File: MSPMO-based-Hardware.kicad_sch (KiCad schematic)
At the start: 0 parts

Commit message: created MSPMOG3507SPTR symbol
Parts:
- added U1: ~, Package_QFP:LQFP-48-1EP_7x7mm_P0.5mm_EP3.6x3.6mm_ThermalVias, symbol MSPMOG3507SPTR:MSPMOG3507SPTR
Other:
- title: Schematic-1 -> MSPMO-Hardware
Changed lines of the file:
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@@
 	(paper "A4")
 	(title_block
-		(title "Schematic-1")
-		(date "2026-02-09")
+		(title "MSPMO-Hardware")
+		(date "2026-02-16")
 		(company "Odari-Designs")
 	)
+	(symbol
+		(lib_id "MSPMOG3507SPTR:MSPMOG3507SPTR")
+		(at 133.35 50.8 0)
+		(unit 1)
+		(exclude_from_sim no)
+		(in_bom yes)
+		(on_board yes)
+		(dnp no)
+		(property "Reference" "U1"
+			(at 175.514 102.616 0)
+			(effects
+				(font
+					(size 1.27 1.27)
+				)
+				(justify left)
+			)
+		)
+		(property "Value" "~"
+			(at 150.7333 139.7 0)
+			(effects
+				(font
+					(size 1.27 1.27)
+				)
+				(justify left)
+			)
+		)
+		(property "Footprint" "Package_QFP:LQFP-48-1EP_7x7mm_P0.5mm_EP3.6x3.6mm_ThermalVias"
+			(at 133.35 50.8 0)
+			(effects
+				(font
+					(size 1.27 1.27)
+				)
+				(hide yes)
+			)
+		)
+		(property "Datasheet" "https://www.ti.com/lit/ds/symlink/mspm0g3507.pdf?ts=1771244205042&ref_url=https%253A%252F%252Fwww.ti.com%252Fproduct%252FMSPM0G3507%252Fpart-details%252FMSPM0G3507SPTR"
+			(at 133.35 50.8 0)
+			(effects
+				(font
+					(size 1.27 1.27)
+				)
+				(hide yes)
+			)
+		)
+		(property "Description" "Microcontroller ARM Cortex -MO +80Mhz 128kB 32kb"
+			(at 133.35 50.8 0)
+			(effects
+				(font
+					(size 1.27 1.27)
+				)
+				(hide yes)
+			)
+		)
+		(property "Manufacturer" "Texas Instruments"
+			(at 133.35 50.8 0)
+			(effects
+				(font
+					(size 1.27 1.27)
+				)
+				(hide yes)
+			)
+		)
+		(property "Manufacturer Part Number" "MSPMOG3507SPTR"
+			(at 133.35 50.8 0)
+			(effects
+				(font
+					(size 1.27 1.27)
+				)
+				(hide yes)
+			)
+		)
+		(property "Distributor Link 1" "https://eu.mouser.com/ProductDetail/Texas-Instruments/MSPM0G3507SPTR?qs=ST9lo4GX8V1GEI0H4GAJcA%3D%3D&srsltid=AfmBOorHTAR3Xy9xSr2ftDIAS1bj25rc6j3AfXq4hEl9akMYmwlnfI_u"
+			(at 133.35 50.8 0)
+			(effects
+				(font
+					(size 1.27 1.27)
+				)
+				(hide yes)
+			)
+		)
+		(property "Distributor Link 2" "https://www.ti.com/product/MSPM0G3507/part-details/MSPM0G3507SPTR"
+			(at 133.35 50.8 0)
+			(effects
+				(font
+					(size 1.27 1.27)
+				)
+				(hide yes)
+			)
+		)
+		(property "LCSC" "C22362630"
+			(at 133.35 50.8 0)
+			(effects
+				(font
+					(size 1.27 1.27)
+				)
+				(hide yes)
+			)
+		)
+		(pin "4"
+		)
+		(pin "42"
+		)
+		(pin "8"
+		)
+		(pin "9"
+		)
+		(pin "30"
+		)
+		(pin "34"
+		)
+		(pin "18"
+		)
+		(pin "40"
+		)
+		(pin "16"
+		)
+		(pin "47"
+		)
+		(pin "33"
+		)
+		(pin "12"
+		)
+		(pin "6"
+		)
+		(pin "14"
+		)
+		(pin "2"
+		)
+		(pin "1"
+		)
+		(pin "10"
+		)
+		(pin "17"
+		)
+		(pin "11"
+		)
+		(pin "28"
+		)
+		(pin "13"
+		)
+		(pin "29"
+		)
+		(pin "31"
+		)
+		(pin "32"
+		)
+		(pin "35"
+		)
+		(pin "39"
+		)
+		(pin "42"
+		)
+		(pin "44"
+		)
+		(pin "45"
+		)
+		(pin "46"
+		)
+		(pin "3"
+		)
+		(pin "31"
+		)
+		(pin "7"
+		)
+		(pin "48"
+		)
+		(pin "15"
+		)
+		(pin "20"
+		)
+		(pin "23"
+		)
+		(pin "24"
+		)
+		(pin "25"
+		)
+		(pin "36"
+		)
+		(pin "37"
+		)
+		(pin "22"
+		)
+		(pin "26"
+		)
+		(pin "37"
+		)
+		(pin "41"
+		)
+		(pin "21"
+		)
+		(instances
+			(project ""
+				(path "/47275325-20e8-4d07-a4a0-f2c0cd8b78a7"
+					(reference "U1")
+					(unit 1)
+				)
+			)
+		)
+	)
 	(sheet_instances

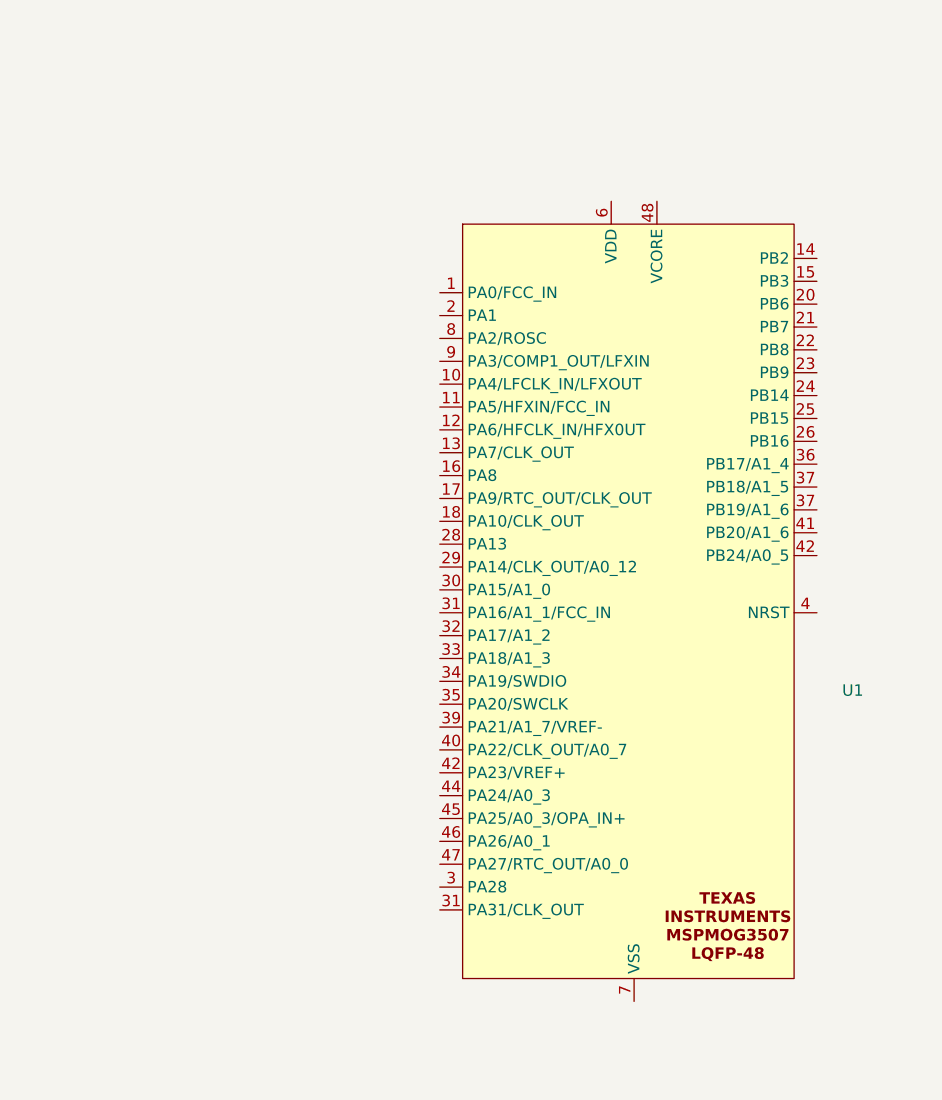
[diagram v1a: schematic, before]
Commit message: chore(hardware): add passive components and update BOM configuration
Add capacitors (C1-C6), resistors (R1-R3), and crystal (X1) to the MSPM0G3507 schematic with associated power decoupling and filtering circuitry. Update BOM export path to Docs folder and add distributor/manufacturer fields to bill of materials configuration.
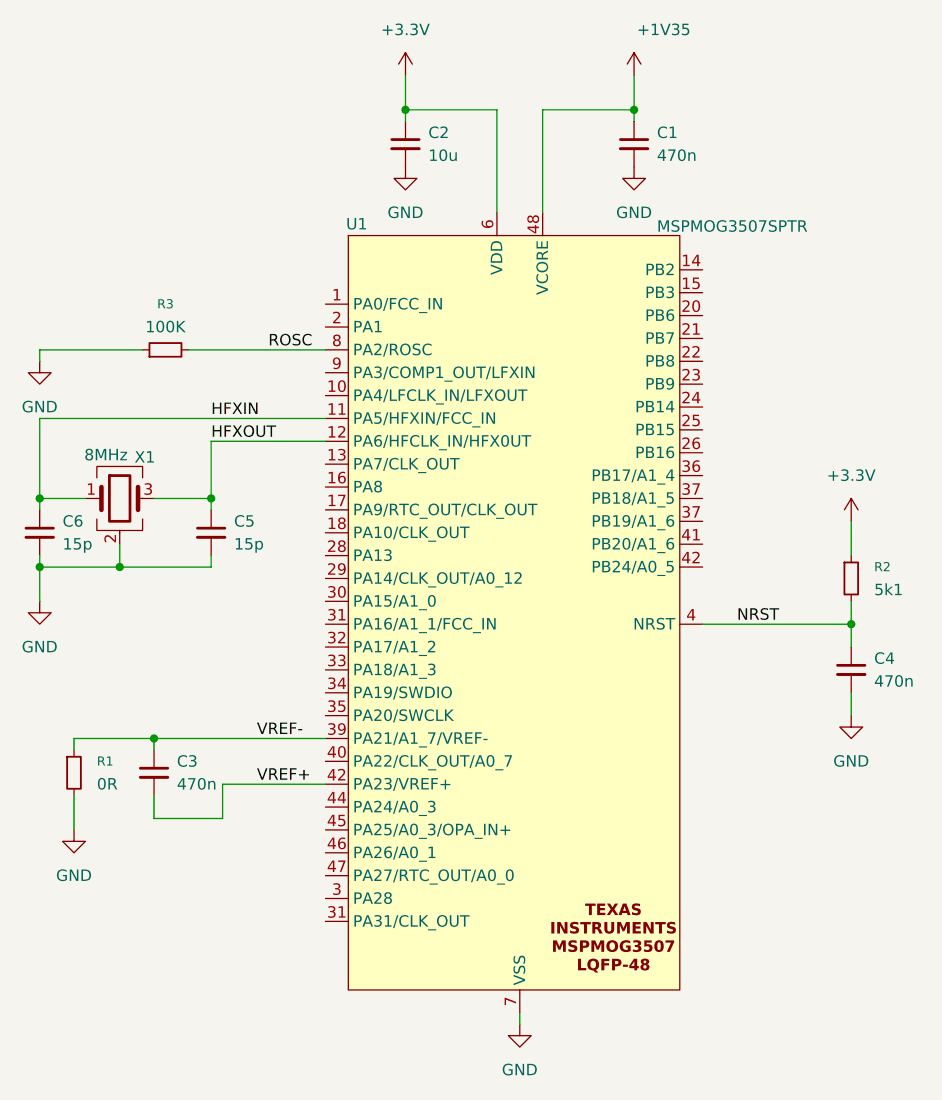
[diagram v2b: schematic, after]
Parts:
- added C1, C3, C4: 470n, Capacitor_SMD:C_0805_2012Metric, symbol Device:C_Small
- added C2: 10u, Capacitor_SMD:C_0805_2012Metric, symbol Device:C_Small
- added C5, C6: 15p, Capacitor_SMD:C_0805_2012Metric, symbol Device:C_Small
- added R1: 0R, Resistor_SMD:R_0603_1608Metric, symbol Device:R_Small
- added R2: 5k1, Resistor_SMD:R_0603_1608Metric, symbol Device:R_Small
- added R3: 100K, Resistor_SMD:R_0603_1608Metric, symbol Device:R_Small
- added X1: 8MHz, Crystal:Crystal_SMD_3225-4Pin_3.2x2.5mm, symbol Device:Crystal_GND24
- U1: value ~ -> MSPMOG3507SPTR
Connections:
- net HFXIN: now reaches U1.11 (PA5/HFXIN/FCC_IN)
- net HFXIN: now also C6.1, X1.1
- net HFXOUT: now reaches U1.12 (PA6/HFCLK_IN/HFX0UT)
- net HFXOUT: now also C5.1, X1.3
- net VREF-: now reaches U1.39 (PA21/A1_7/VREF-)
- net VREF-: now also C3.1, R1.1
- net NRST: now reaches U1.4 (NRST)
- net NRST: now also C4.1, R2.2
- net VREF+: now reaches U1.42 (PB24/A0_5)
- net VREF+: now also C3.2
- net +1V35: now reaches U1.48 (VCORE)
- net +1V35: now also C1.1
- net +3.3V: now reaches U1.6 (VDD)
- net +3.3V: now also C2.1, R2.1
- net GND: now reaches U1.7 (VSS)
- net GND: now also C1.2, C2.2, C4.2, C5.2, C6.2, R1.2, R3.1, X1.2 (G), X1.4 (G)
- net ROSC: now reaches U1.8 (PA2/ROSC)
- net ROSC: now also R3.2
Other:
- moved on the sheet: U1

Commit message: update the schematic file
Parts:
- added C10, C7, C8: 470n, Capacitor_SMD:C_0805_2012Metric, symbol Device:C_Small
- added C9: 10u, Capacitor_SMD:C_0805_2012Metric, symbol Device:C_Small
- added J2: USB_C_Receptacle_USB2.0_16P, Connector_USB:USB_C_Receptacle_GCT_USB4105-xx-A_16P_TopMnt_Horizontal, symbol Connector:USB_C_Receptacle_USB2.0_16P
- added R4: 0R, Resistor_SMD:R_0603_1608Metric, symbol Device:R_Small
- added R5, R6: 5k1, Resistor_SMD:R_0603_1608Metric, symbol Device:R_Small
- added U2: USBLC6-2SC6, Package_TO_SOT_SMD:SOT-23-6, symbol Power_Protection:USBLC6-2SC6
- added U3: SPX3819M5-L-3-3, Package_TO_SOT_SMD:SOT-23-5, symbol Regulator_Linear:SPX3819M5-L-3-3
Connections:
- net +3.3V: now also C9.1, U3.5 (OUT)
- net GND: now also C10.2, C7.2, C8.2, C9.2, J2.A1 (GND), J2.A12 (GND), J2.B1 (GND), J2.B12 (GND), J2.S1 (SHIELD), R5.2, R6.2, U2.2 (GND), U3.2 (GND)
- new net: J2.A7 (D-), J2.B7 (D-), U2.1 (I/O1)
- new net: J2.A6 (D+), J2.B6 (D+), U2.3 (I/O2)
- new net: C10.1, U3.4 (BP)
- new net +5V: C8.1, R4.2, U3.1 (IN), U3.3 (EN)
- new net +VBUS: C7.1, J2.A4 (VBUS), J2.A9 (VBUS), J2.B4 (VBUS), J2.B9 (VBUS), R4.1, U2.5 (VBUS)
- new net USBD+: J2.B5 (CC2), R5.1
- new net USBD-: J2.A5 (CC1), R6.1
- no-connect marks 0 -> 2
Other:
- note added: "MICROCONTROLLER"
- note added: "REGULATOR 3.3V"
- note added: "USB_C"
- moved on the sheet: C1, C2, C3, C4, C5, C6, R1, R2, R3, U1, X1

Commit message: update the schematic file
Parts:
- J2: Distributor Link 1 (none) -> https://eu.mouser.com/ProductDetail/Amphenol-Commercial-Pro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; Distributor Link 2 (none) -> https://www.digikey.com/en/products/detail/amphenol-cs-comm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; LCSC (none) -> C20657289; Manufacturer (none) -> Amphenol Commercial Products; Manufacturer part Number (none) -> GSB1C4621DS1HR
- U2: Distributor Link 1 (none) -> https://eu.mouser.com/ProductDetail/STMicroelectronics/USBL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; Distributor Link 2 (none) -> https://www.digikey.com/en/products/detail/stmicroelectroni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; LCSC (none) -> C2969755; Manufacturer (none) -> STMicroelectronics; Manufacturer part Number (none) -> USBLC6-2SC6Y
- U3: Distributor Link 1 (none) -> https://eu.mouser.com/ProductDetail/MaxLinear/SPX3819M5-L-3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; Distributor Link 2 (none) -> https://eu.mouser.com/ProductDetail/MaxLinear/SPX3819M5-L-3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; LCSC (none) -> https://www.digikey.com/en/products/detail/maxlinear-inc/SP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; Manufacturer (none) -> MaxLinear; Manufacturer part Number (none) -> SPX3819M5-L-3-3/TR
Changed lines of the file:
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@@
 			)
 		)
-		(property "Datasheet" "https://www.st.com/resource/en/datasheet/usblc6-2.pdf"
+		(property "Datasheet" "https://www.st.com/resource/en/datasheet/usblc6-2sc6y.pdf"
 			(at 73.66 50.165 0)
 			(effects
@@
 			)
 		)
-		(property "Description" "Very low capacitance ESD protection diode, 2 data-line, SOT-23-6"
+		(property "Description" "ESD Protection Diodes / TVS Diodes 2 Line 2.5pF 10nA USB 2.0 Automotive"
+			(at 72.39 41.91 0)
+			(effects
+				(font
+					(size 1.27 1.27)
+				)
+				(hide yes)
+			)
+		)
+		(property "Manufacturer" "STMicroelectronics"
+			(at 72.39 41.91 0)
+			(effects
+				(font
+					(size 1.27 1.27)
+				)
+				(hide yes)
+			)
+		)
+		(property "Manufacturer part Number" "USBLC6-2SC6Y"
+			(at 72.39 41.91 0)
+			(effects
+				(font
+					(size 1.27 1.27)
+				)
+				(hide yes)
+			)
+		)
+		(property "Distributor Link 1" "https://eu.mouser.com/ProductDetail/STMicroelectronics/USBLC6-2SC6Y?qs=gNDSiZmRJS%2FOgDexvXkdow%3D%3D"
+			(at 72.39 41.91 0)
+			(effects
+				(font
+					(size 1.27 1.27)
+				)
+				(hide yes)
+			)
+		)
+		(property "Distributor Link 2" "https://www.digikey.com/en/products/detail/stmicroelectronics/USBLC6-2SC6Y/2819177?s=N4IgTCBcDaIKoGUBCAZAwgNgLRgZgmiALoC%2BQA"
+			(at 72.39 41.91 0)
+			(effects
+				(font
+					(size 1.27 1.27)
+				)
+				(hide yes)
+			)
+		)
+		(property "LCSC" "C2969755"
 			(at 72.39 41.91 0)
 			(effects
@@
 			)
 		)
-		(property "Datasheet" "https://www.usb.org/sites/default/files/documents/usb_type-c.zip"
+		(property "Datasheet" "https://cdn.amphenol-cs.com/media/wysiwyg/files/drawing/gsb1c46x1ds1hr.pdf"
 			(at 41.91 49.53 0)
 			(effects
@@
 			)
 		)
-		(property "Description" "USB 2.0-only 16P Type-C Receptacle connector"
+		(property "Description" "USB Connectors USB2.0 TYPE C"
+			(at 38.1 49.53 0)
+			(effects
+				(font
+					(size 1.27 1.27)
+				)
+				(hide yes)
+			)
+		)
+		(property "Manufacturer" "Amphenol Commercial Products"
+			(at 38.1 49.53 0)
+			(effects
+				(font
+					(size 1.27 1.27)
+				)
+				(hide yes)
+			)
+		)
+		(property "Manufacturer part Number" "GSB1C4621DS1HR"
+			(at 38.1 49.53 0)
+			(effects
+				(font
+					(size 1.27 1.27)
+				)
+				(hide yes)
+			)
+		)
+		(property "Distributor Link 1" "https://eu.mouser.com/ProductDetail/Amphenol-Commercial-Products/GSB1C4621DS1HR?qs=3Rah4i%252BhyCGuNOeu2qbG9g%3D%3D"
+			(at 38.1 49.53 0)
+			(effects
+				(font
+					(size 1.27 1.27)
+				)
+				(hide yes)
+			)
+		)
+		(property "Distributor Link 2" "https://www.digikey.com/en/products/detail/amphenol-cs-commercial-products/GSB1C4621DS1HR/21623859?s=N4IgTCBcDaIOIGUBCBGAwgFgGxhQEQRQAkAlEAXQF8g"
+			(at 38.1 49.53 0)
+			(effects
+				(font
+					(size 1.27 1.27)
+				)
+				(hide yes)
+			)
+		)
+		(property "LCSC" "C20657289"
 			(at 38.1 49.53 0)
 			(effects
@@
 			)
 		)
-		(property "Datasheet" "https://www.exar.com/content/document.ashx?id=22106&languageid=1033&type=Datasheet&partnumber=SPX3819&filename=SPX3819.pdf&part=SPX3819"
+		(property "Datasheet" "https://www.maxlinear.com/ds/SPX3819.pdf"
 			(at 45.72 113.03 0)
 			(effects
@@
 			)
 		)
-		(property "Description" "500mA Low drop-out regulator, Fixed Output 3.3V, SOT-23-5"
+		(property "Description" "LDO Voltage Regulators 500mA LOW NOISE LDO"
 			(at 45.72 113.03 0)
 			(effects
+				(font
+					(size 1.27 1.27)
+				)
+				(hide yes)
+			)
+		)
+		(property "Manufacturer" "MaxLinear"
+			(at 45.72 113.03 0)
+			(effects
+				(font
+					(size 1.27 1.27)
+				)
+				(hide yes)
+			)
+		)
+		(property "Manufacturer part Number" "SPX3819M5-L-3-3/TR"
+			(at 45.72 113.03 0)
+			(effects
+				(font
+					(size 1.27 1.27)
+				)
+				(hide yes)
+			)
+		)
+		(property "Distributor Link 1" "https://eu.mouser.com/ProductDetail/MaxLinear/SPX3819M5-L-3-3-TR?qs=S%2FCBhQS5rCp1Bb7a%252BD%2FCBQ%3D%3D"
+			(at 45.72 113.03 0)
+			(effects
+				(font
+					(size 1.27 1.27)
+				)
+				(hide yes)
+			)
+		)
+		(property "Distributor Link 2" "https://eu.mouser.com/ProductDetail/MaxLinear/SPX3819M5-L-3-3-TR?qs=S%2FCBhQS5rCp1Bb7a%252BD%2FCBQ%3D%3D"
+			(at 45.72 113.03 0)
+			(effects
+				(font
+					(size 1.27 1.27)
+				)
+				(hide yes)
+			)
+		)
+		(property "LCSC" "https://www.digikey.com/en/products/detail/maxlinear-inc/SPX3819M5-L-3-3-TR/2472394?s=N4IgTCBcDaIMoAUAaBmAHARgJwFkCsAtADIEqkD0AKgEogC6AvkA"
+			(at 45.72 113.03 0)
+			(effects

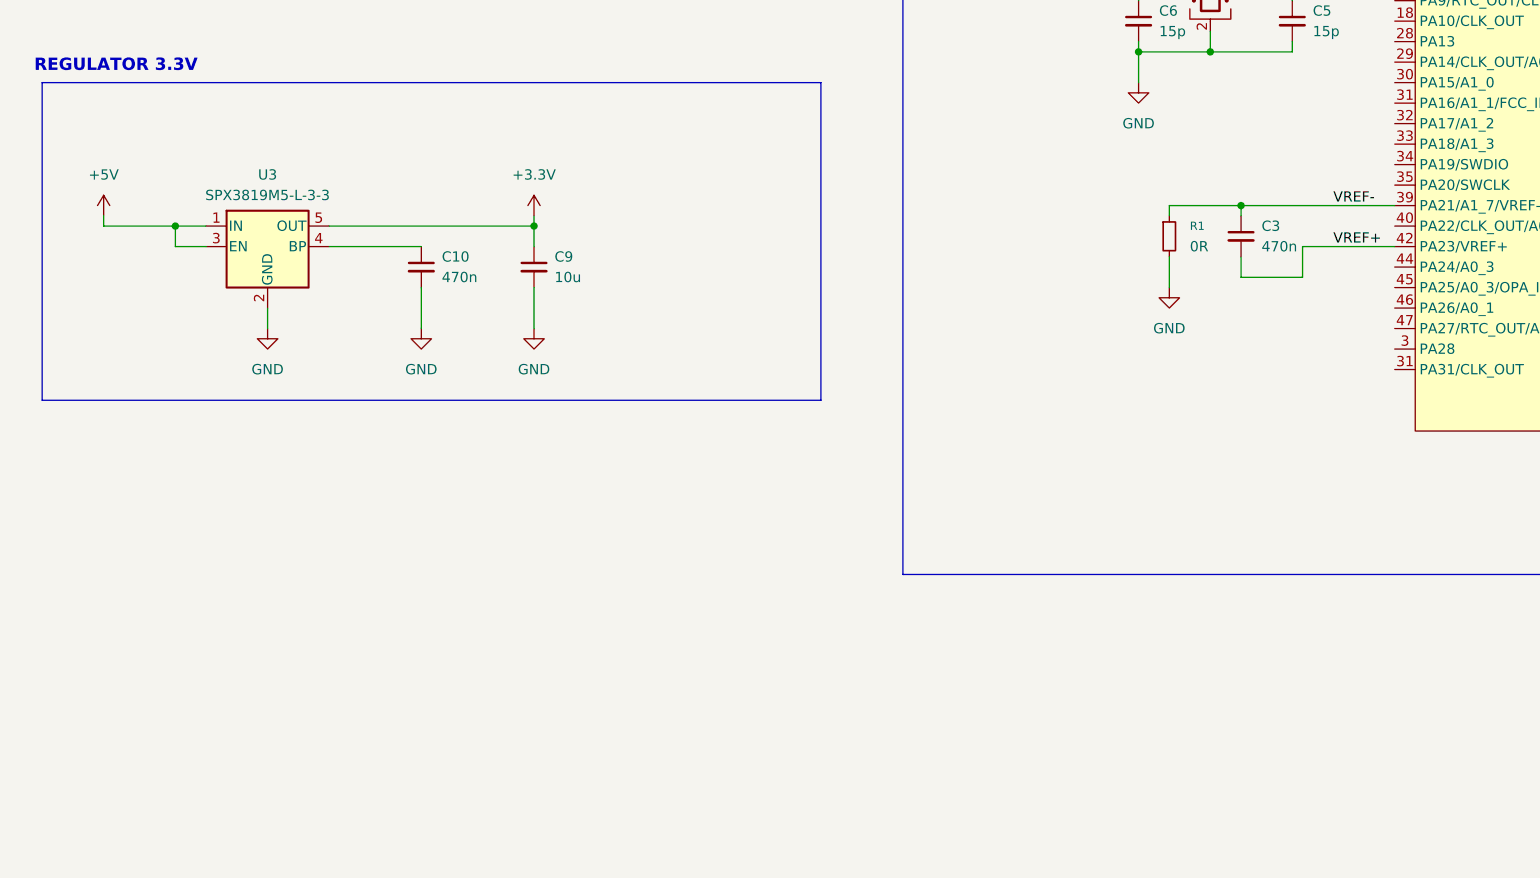
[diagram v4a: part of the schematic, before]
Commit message: Update:add TC2030 for debugging interface
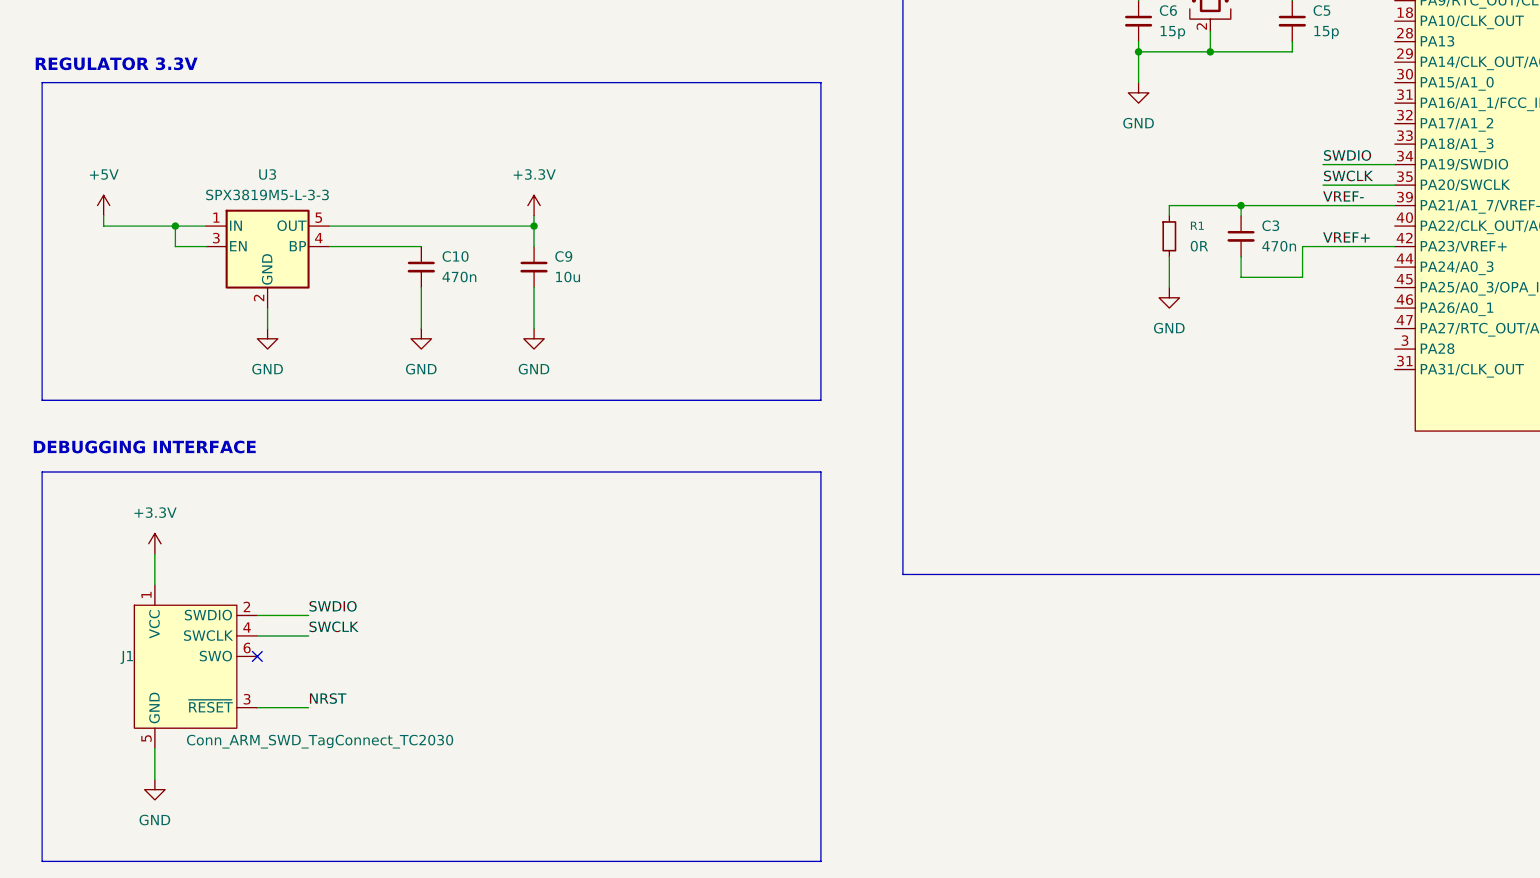
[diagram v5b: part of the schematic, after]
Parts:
- added J1: Conn_ARM_SWD_TagConnect_TC2030, Connector:Tag-Connect_TC2030-IDC-FP_2x03_P1.27mm_Vertical, symbol Connector:Conn_ARM_SWD_TagConnect_TC2030
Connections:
- net +3.3V: now also J1.1 (VCC)
- net GND: now also J1.5 (GND)
- net NRST: now also J1.3 (~{RESET})
- net SWDIO: now reaches U1.34 (PA19/SWDIO)
- net SWDIO: now also J1.2 (SWDIO)
- net SWCLK: now reaches U1.35 (PA20/SWCLK)
- net SWCLK: now also J1.4 (SWCLK)
- no-connect marks 2 -> 3
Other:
- note added: "DEBUGGING INTERFACE"
